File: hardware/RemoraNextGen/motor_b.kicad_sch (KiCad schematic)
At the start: 33 parts, among them J6 Motor B phase U, J7 Motor B phase V, J8 Motor B phase W, Q10 CSD16327Q3, Q11 CSD16327Q3, Q12 CSD16327Q3, Q13 CSD16327Q3, Q8 CSD16327Q3, Q9 CSD16327Q3, U6 DRV8300D (B), U7 INA180A2

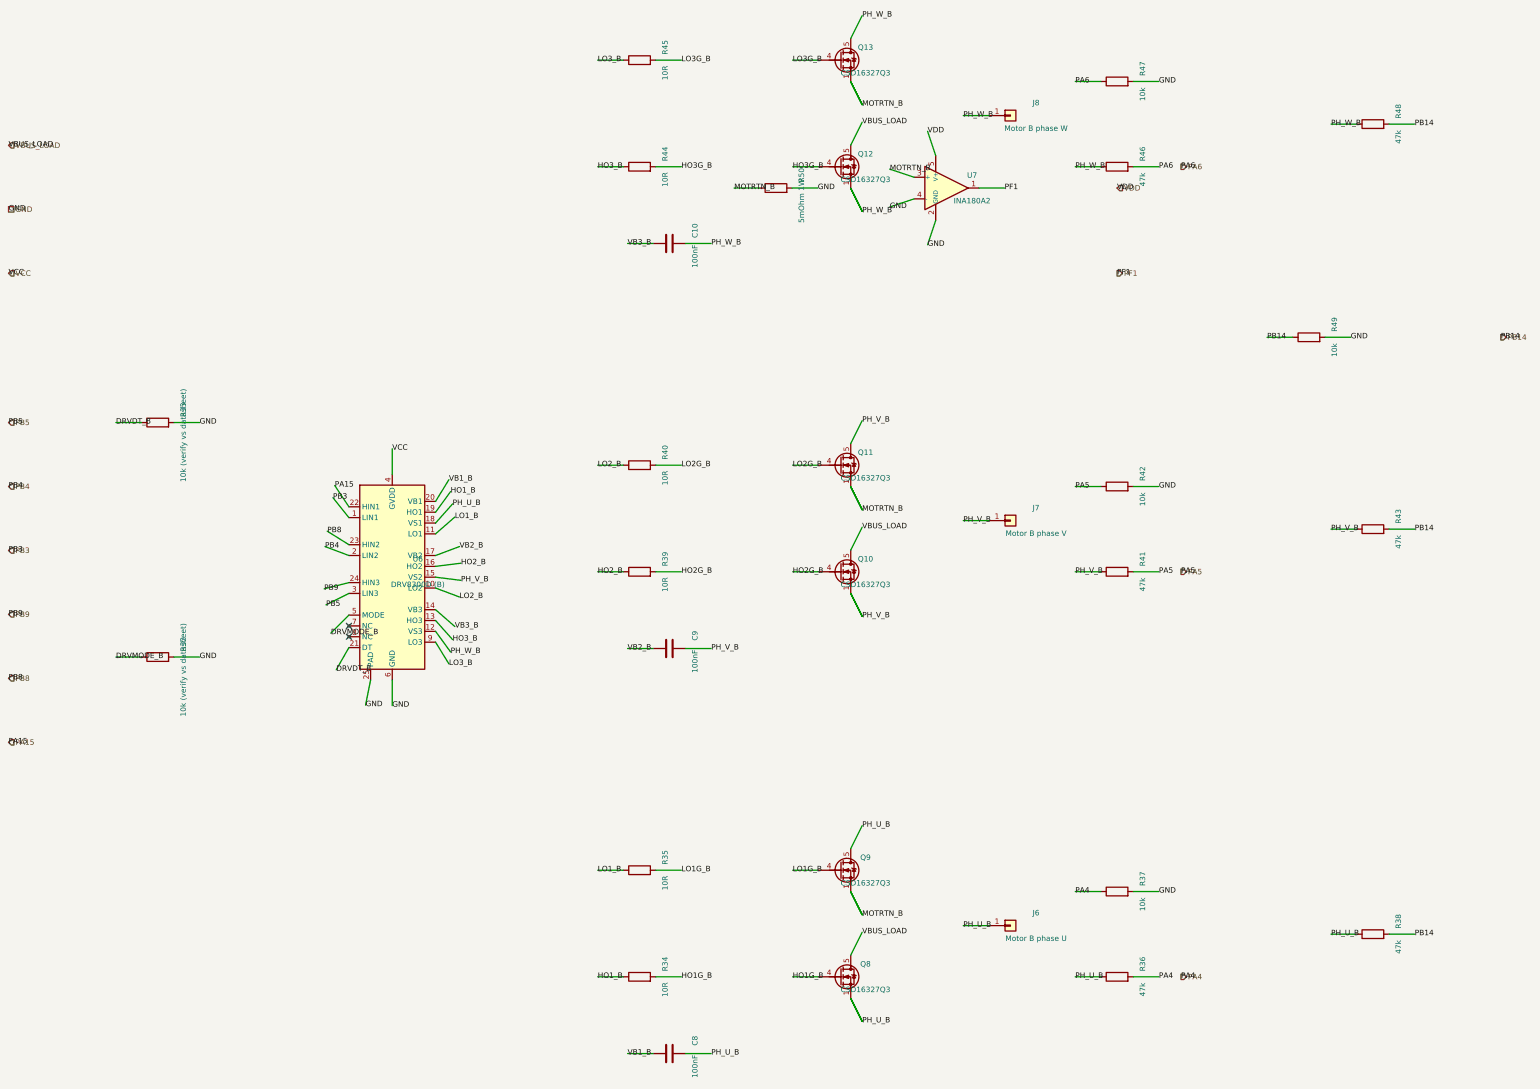
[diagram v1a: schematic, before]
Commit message: Draw real wires instead of floating labels; fix Nucleo lane overlap
Two readability problems, found by actually rendering the generated
schematics to SVG and inspecting them:

- On the root sheet, the 26 Nucleo GPIO/power signals were routed as
  parallel lanes only 4mm apart, each running the full page height.
  ERC was clean, but at any normal zoom they visually merged into an
  unreadable cable bundle. Lanes are now grouped one bundle per
  destination sheet (Power/Motor A/Motor B), with wider in-group
  spacing and a visible gap between groups, sized programmatically
  instead of hardcoded.

- On the power/motor sheets, nearly every net - even between two
  physically adjacent components - was drawn as two disconnected
  stub-wire-and-label islands relying purely on same-name matching,
  never an actual wire. net() now defers to a finalize_nets() pass:
  a net touched at exactly two points gets a real drawn wire (jogged
  if needed); a net touched at 3+ points (GND, VCC, VDD and other
  genuinely pervasive rails) keeps the label convention, matching how
  a real schematic handles shared rails.

Caught a real bug in the first pass at the second fix: a naive
2-segment jog's corner landed exactly on an unrelated VDD hier_label,
silently shorting a motor's current-sense output onto the shared VDD
rail. Fixed by routing jogs through a grid-snapped midpoint instead of
a corner shared with either endpoint's own row/column.

Also ignores *-backups/ (KiCad's own local backup zips).

Co-Authored-By: Claude Sonnet 5 <noreply@anthropic.com>
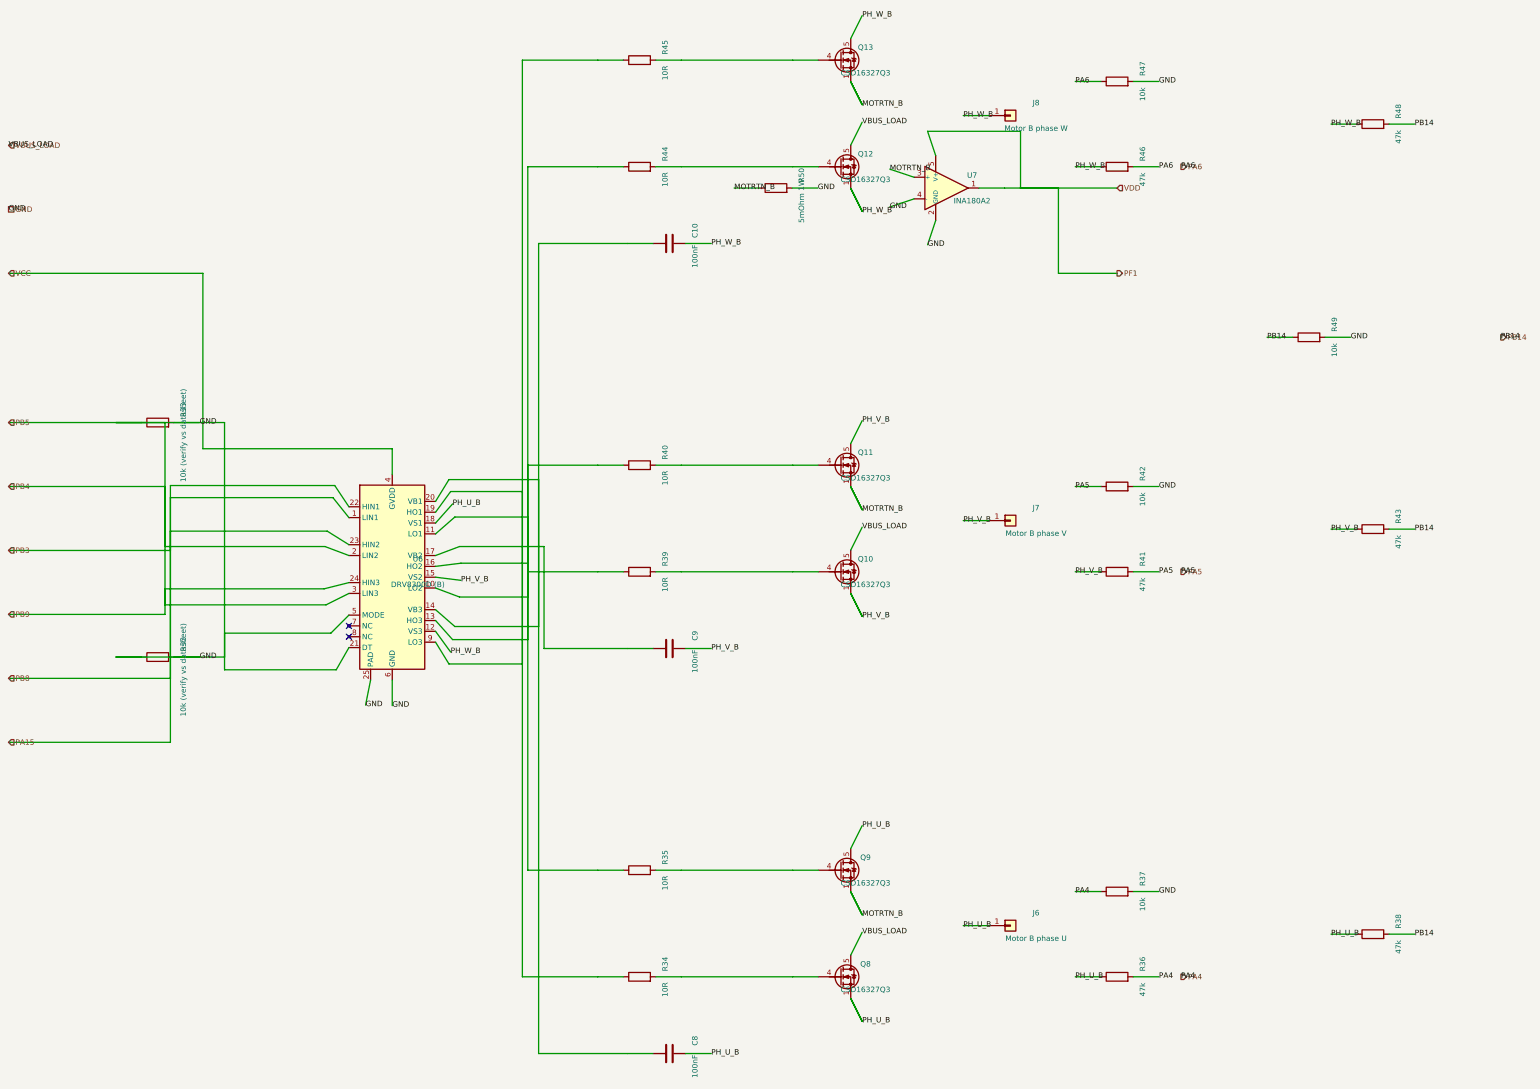
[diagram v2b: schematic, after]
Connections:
- net DRVDT_B is gone; now on net GND: R33.1, U6.21 (DT)
- net DRVMODE_B is gone; now on net GND: R32.1, U6.5 (MODE)
- net HO3_B is gone; now on an unnamed net: R44.1, U6.13 (HO3)
- net LO1_B is gone; now on an unnamed net: R35.1, U6.11 (LO1)
- net LO2_B is gone; now on an unnamed net: R40.1, U6.10 (LO2)
- net LO3_B is gone; now on an unnamed net: R45.1, U6.9 (LO3)
- net PB3 is gone; now on net PA15: U6.1 (LIN1)
- net PB4 is gone; now on net GND: U6.2 (LIN2)
- net PB5 is gone; now on net GND: U6.3 (LIN3)
- net PB8 is gone; now on net PA15: U6.23 (HIN2)
- net PB9 is gone; now on net GND: U6.24 (HIN3)
- net VB3_B is gone; now on an unnamed net: C10.1, U6.14 (VB3)
- net VDD is gone; now on net PF1: U7.5 (V+)
- net HO1G_B: no longer names the net of Q8.4 (G), R34.2
- net HO1_B: no longer names the net of R34.1, U6.19 (HO1)
- net HO2G_B: no longer names the net of Q10.4 (G), R39.2
- net HO2_B: no longer names the net of R39.1, U6.16 (HO2)
- net HO3G_B: no longer names the net of Q12.4 (G), R44.2
- net LO1G_B: no longer names the net of Q9.4 (G), R35.2
- net LO2G_B: no longer names the net of Q11.4 (G), R40.2
- net LO3G_B: no longer names the net of Q13.4 (G), R45.2
- net VB1_B: no longer names the net of C8.1, U6.20 (VB1)
- net VB2_B: no longer names the net of C9.1, U6.17 (VB2)

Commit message: Fit sub-sheet blocks on the page; wire local nets in power schematic
Motor B's sheet box ran from y=610 to y=1010, but the A0 landscape root
page is only 841mm tall - it silently overflowed the bottom edge by
169mm. Motor A/B's box heights (400mm) were also far bigger than their
actual pin content needs (~240mm). Tightened both to 260mm and now
compute each sheet's Y position from the previous one's bottom edge
plus a fixed gap, instead of hardcoded absolute numbers, so this can't
drift out of sync with the page again.

finalize_nets() previously only drew a real wire for nets with exactly
2 points, so every net touched at 3+ points - the majority of the
power schematic - stayed as disconnected floating labels. Now any net
whose points stay within a 150mm span gets chained together with real
wire regardless of point count; only genuinely page-wide rails (GND,
VCC, VDD, VBUS, and similarly wide-spanning nets like a motor's phase
node or return net) still fall back to labels, matching how a real
schematic handles shared rails. Verified motor_a/b's wide nets still
correctly fall back to labels rather than turning into a new rats-nest.

ERC still 0 errors throughout.

Also ignores ~*.lck (KiCad's file-open lock markers).

Co-Authored-By: Claude Sonnet 5 <noreply@anthropic.com>
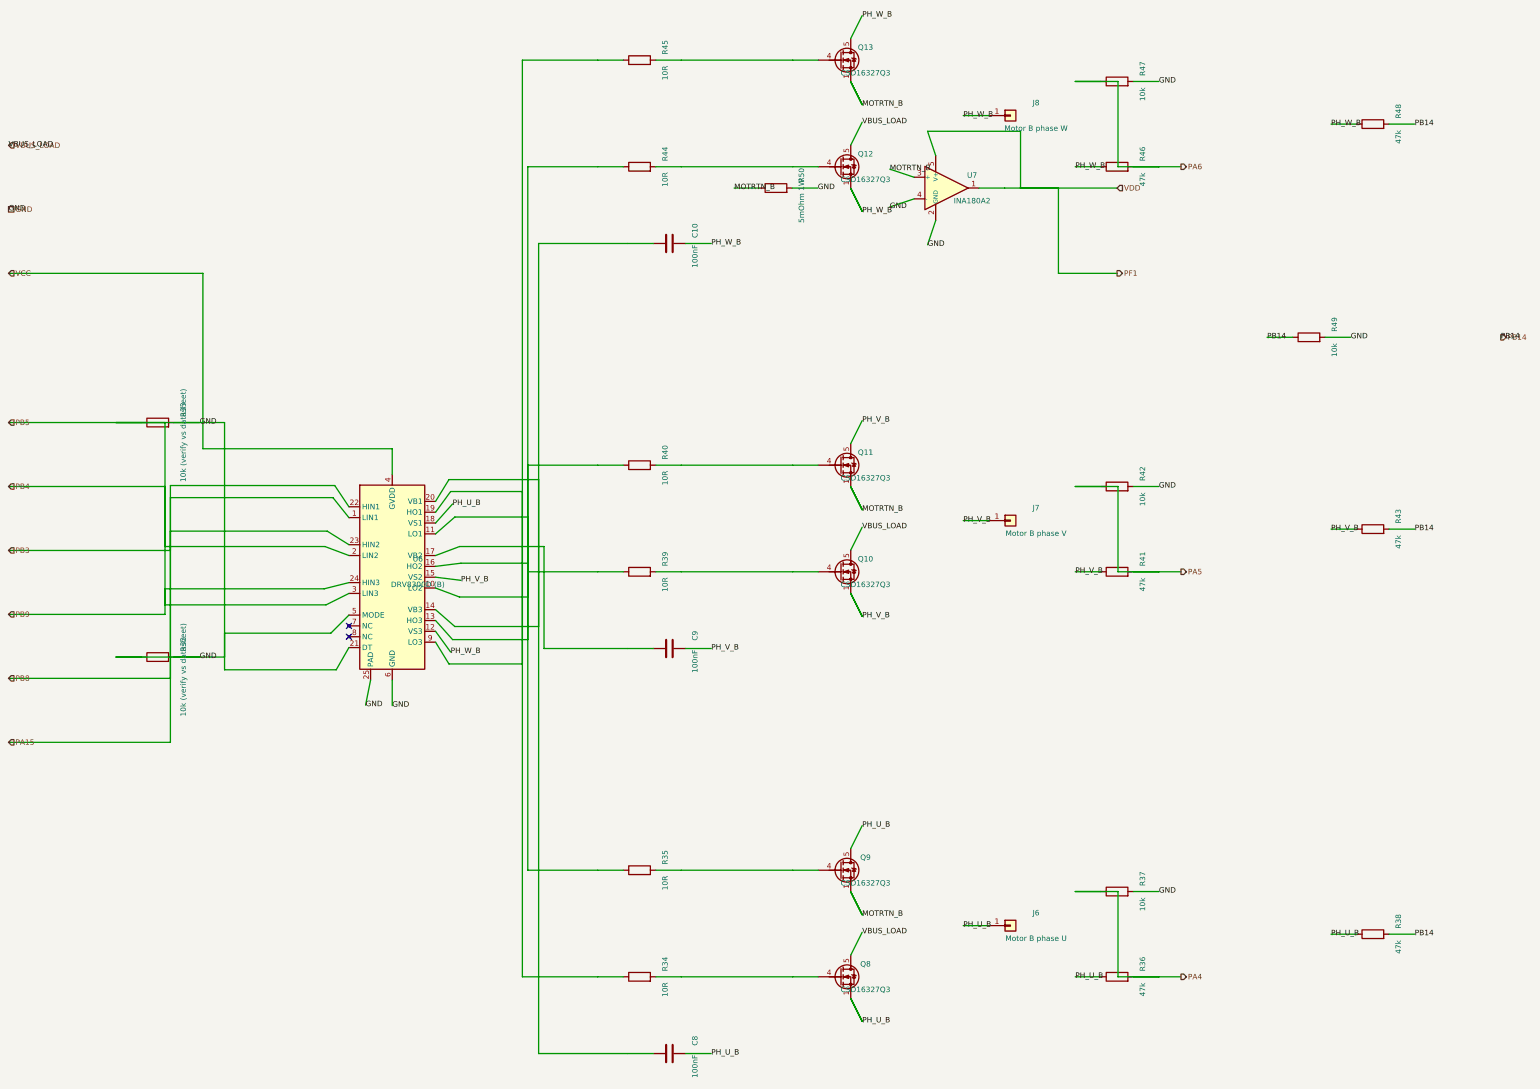
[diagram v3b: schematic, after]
